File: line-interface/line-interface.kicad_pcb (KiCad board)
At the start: 2 copper layers, 80 x 49 mm, 35 parts, among them IC1 ATTINY441-SSU, J1 CONN_01X06, P1 CONN_02X03, P2 CONN_01X04, Q1 NDT2955, U1 LR12K, U2 SN65HVD72, X1 16MHz

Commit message: Finish routing the board, manufacturing order sent
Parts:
- added D7: D, Diodes_SMD:D_SOD-123, F.Cu at (120.3, 118.5)
- added R10: 10k, Resistors_SMD:R_0603, F.Cu at (104.5, 124.5)
- added R9: 10k, Resistors_SMD:R_0603, F.Cu at (104.5, 122.0)
- moved R6 34.7 mm to (104.5, 119.5), turned to 180 degrees
- moved R2 34.3 mm to (132.5, 115.8), turned to 90 degrees
- moved C2 28.0 mm to (147.0, 117.0)
- moved C3 28.0 mm to (129.0, 105.0)
- moved C5 28.0 mm to (119.0, 102.0)
- moved D1 28.0 mm to (144.0, 125.0)
- moved D2 28.0 mm to (146.0, 113.0)
- moved D6 28.0 mm to (112.0, 109.0)
- moved MK1 28.0 mm to (148.0, 145.0)
- moved MK4 28.0 mm to (148.0, 104.0)
- moved P2 28.0 mm to (149.1, 130.0)
- moved Q1 28.0 mm to (135.7, 108.3)
- moved R5 28.0 mm to (114.0, 107.0)
- moved R7 28.0 mm to (114.0, 111.1)
- moved R8 28.0 mm to (112.0, 112.0)
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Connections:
- net /EXCITATION renamed Net-(IC1-Pad5)
- D5 pad 1: GND -> Net-(D4-Pad2)
- D5 pad 2: Net-(D5-Pad2) -> +5V
- IC1 pad 6: Net-(IC1-Pad6) -> /~CS
- P2 pad 2: /RS485A -> /RS485B
- P2 pad 3: /RS485B -> /RS485A
- R3 pad 2: Net-(IC1-Pad6) -> Net-(IC1-Pad10)
- R6 pad 1: Net-(D5-Pad2) -> /MISO
- R6 pad 2: Net-(IC1-Pad10) -> /SERIAL_DATA_IN
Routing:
- net +5V: track 0.00 -> 109.1 mm, vias 0 -> 2
- net /MISO: track 0.00 -> 68.5 mm
- net /SCK: track 0.00 -> 67.2 mm
- net /~CS: track 0.00 -> 58.6 mm, vias 0 -> 2
- net Net-(C3-Pad1): track 0.00 -> 47.7 mm
- net GND: track 0.00 -> 43.3 mm, vias 0 -> 14
- net /MOSI: track 0.00 -> 27.3 mm
- net Net-(C2-Pad1): track 0.00 -> 23.0 mm
- net /RESET: track 0.00 -> 19.7 mm, vias 0 -> 2
- net Net-(C6-Pad1): track 0.00 -> 13.4 mm
- net Net-(C8-Pad1): track 0.00 -> 13.3 mm
- net Net-(IC1-Pad13): track 0.00 -> 11.7 mm
- net /RS485B: track 0.00 -> 11.5 mm
- net VCC: track 0.00 -> 11.1 mm
- net /RS485A: track 0.00 -> 11.0 mm
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- added copper zone on B.Cu, net GND
- added copper zone on F.Cu, net GND
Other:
- board size 80 x 49 mm -> 52 x 49 mm

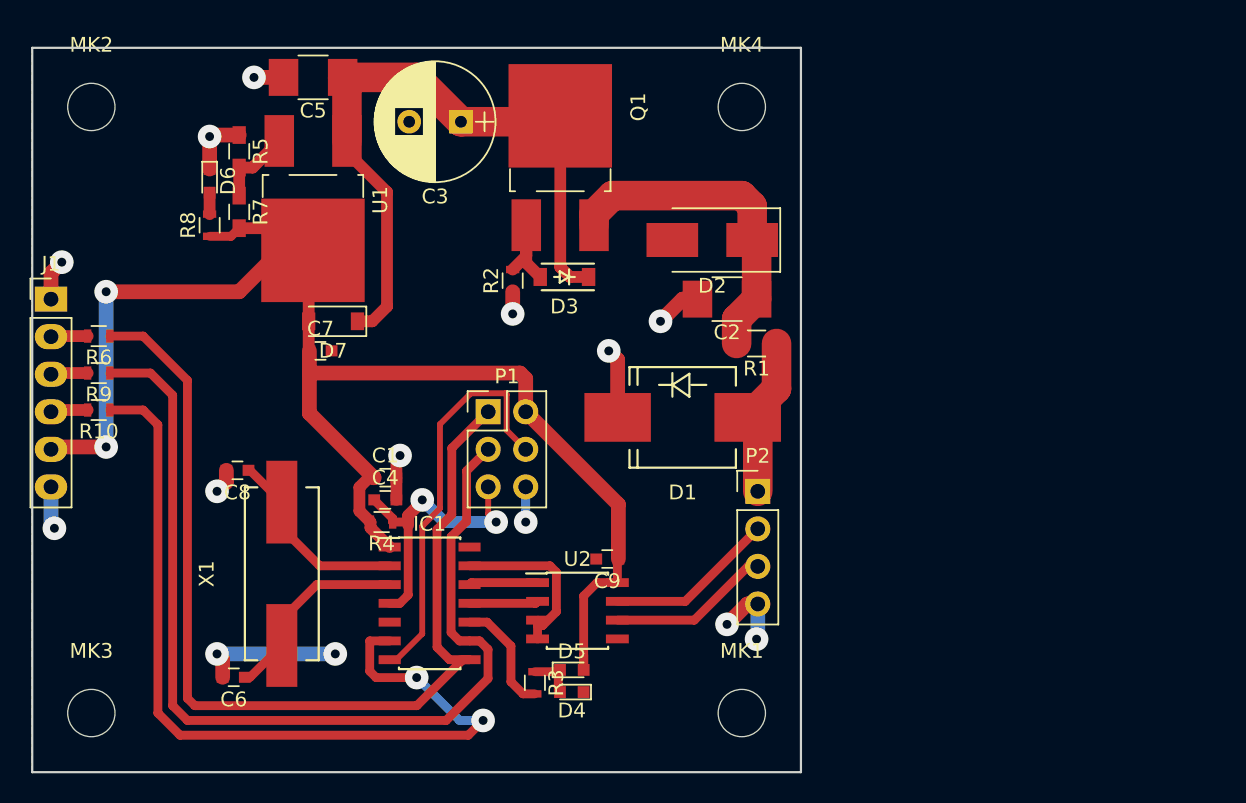
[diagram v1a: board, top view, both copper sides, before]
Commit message: Add firmware of the line sensor, basic stuff -- it spits out sensor data in '1' and '0' ascii strings. Also hardware fixez: * P-channel mosfet has different numbering * a new regulator for power handling capabilities * correct pinout of rs485 transceiver * remove stupid led, what was I thinking?
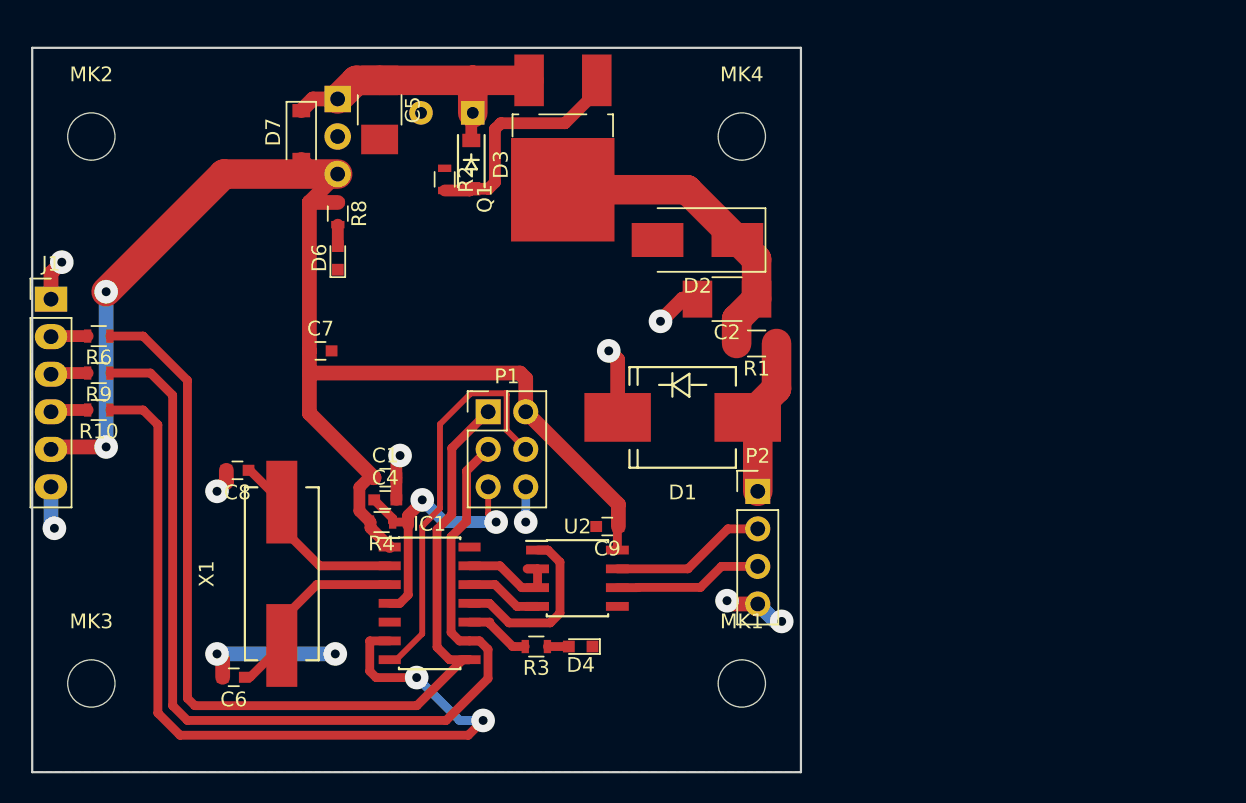
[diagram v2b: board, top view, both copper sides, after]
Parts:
- removed D5: RED, LEDs:LED_0603
- removed R5: 18.2k, Resistors_SMD:R_0603_HandSoldering
- removed R7: 6.04k, Resistors_SMD:R_0603_HandSoldering
- C3: moved to B.Cu
- U1: value LR12K -> LM7805CT; footprint TO_SOT_Packages_SMD:TO-252-2Lead -> TO_SOT_Packages_THT:TO-220_Horizontal; moved to B.Cu
- moved D7 12.8 mm to (118.2, 105.9), turned to 270 degrees
- moved D6 10.1 mm to (120.7, 114.2), turned to 90 degrees
- moved D3 9.87 mm to (129.7, 107.9), turned to 270 degrees
- moved R8 8.71 mm to (120.7, 111.2), turned to 270 degrees
- moved R2 8.25 mm to (127.9, 108.9), turned to 270 degrees
- moved U1 6.75 mm to (120.7, 103.5)
- moved C5 5.01 mm to (123.5, 104.2), turned to 270 degrees
- moved D4 3.14 mm to (137.1, 140.5)
- moved R3 2.45 mm to (134.1, 140.5), turned to 180 degrees
- moved Q1 2.41 mm to (135.9, 105.9), turned to 270 degrees
- moved C9 2.20 mm to (138.9, 132.4)
- moved U2 2.20 mm to (136.9, 135.9)
- moved MK1 2.00 mm to (148.0, 143.0)
- moved MK2 2.00 mm to (104.0, 106.0)
- moved MK3 2.00 mm to (104.0, 143.0)
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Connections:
- Q1 pad 2: Net-(C3-Pad1) -> Net-(C2-Pad1)
- Q1 pad 3: Net-(C2-Pad1) -> Net-(C3-Pad1)
- U1 pad 2: +5V -> GND
- U1 pad 3: Net-(R5-Pad2) -> +5V
- U2 pad 1: Net-(IC1-Pad12) -> Net-(IC1-Pad11)
- U2 pad 2: Net-(IC1-Pad11) -> Net-(IC1-Pad13)
- U2 pad 4: Net-(IC1-Pad13) -> Net-(IC1-Pad12)
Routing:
- net Net-(C3-Pad1): track 47.7 -> 21.1 mm
- net +5V: track 109.1 -> 96.5 mm
- net Net-(D3-Pad2): track 7.27 -> 15.9 mm
- net GND: track 43.3 -> 34.8 mm, vias 14 -> 11
- net Net-(IC1-Pad11): track 4.66 -> 12.2 mm
- net Net-(R5-Pad2): track 5.36 -> 0.00 mm
- net Net-(IC1-Pad13): track 11.7 -> 7.19 mm
- net Net-(IC1-Pad10): track 7.85 -> 4.51 mm
- net Net-(D4-Pad2): track 3.30 -> 1.45 mm
- net Net-(C2-Pad1): track 23.0 -> 21.3 mm
- net Net-(IC1-Pad12): track 4.66 -> 5.92 mm
- net /RS485B: track 11.5 -> 10.6 mm

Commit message: Fix the line interface once more - input resistor has to be rated for 2W, also vias because no hole metallisation
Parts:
- C3: moved to F.Cu
- P2: footprint Pin_Headers:Pin_Header_Straight_1x04_Pitch2.54mm -> Connectors_JST:JST_EH_B04B-EH-A_04x2.50mm_Straight
- R1: footprint Resistors_SMD:R_0805_HandSoldering -> Resistors_SMD:R_2512
- moved R2 16.4 mm to (143.0, 102.5), turned to 90 degrees
- moved D3 12.1 mm to (141.0, 103.5), turned to 90 degrees
- moved R1 6.08 mm to (150.0, 114.0), turned to 90 degrees
- moved D1 3.16 mm to (145.0, 122.0)
- moved D2 3.04 mm to (142.0, 113.5), turned to 270 degrees
- moved C2 2.06 mm to (146.5, 115.0), turned to 270 degrees
- moved P2 1.08 mm to (149.5, 129.0), turned to 270 degrees
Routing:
- net Net-(D3-Pad2): track 15.9 -> 5.75 mm
- net Net-(C3-Pad1): track 21.1 -> 27.6 mm
- net Net-(C2-Pad1): track 21.3 -> 16.4 mm
- net GND: track 34.8 -> 31.0 mm, vias 11 -> 10
- net +5V: track 96.5 -> 98.1 mm
- net VCC: track 11.1 -> 12.2 mm
- net /RS485B: track 10.6 -> 11.5 mm, vias 0 -> 1
- net /RS485A: track 10.8 -> 11.0 mm, vias 0 -> 1
